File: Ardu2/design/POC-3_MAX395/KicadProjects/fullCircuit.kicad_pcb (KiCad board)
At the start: 2 copper layers, 179.3 x 143.5 mm, 131 parts, among them P1 CONN_01X02, P2 CONN_01X14, P3 CONN_01X14, P4 CONN_01X01, P7 CONN_01X15, U1 Pyboard, U10 MAX395, U11 MAX395, U12 MAX395, U13 MAX395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

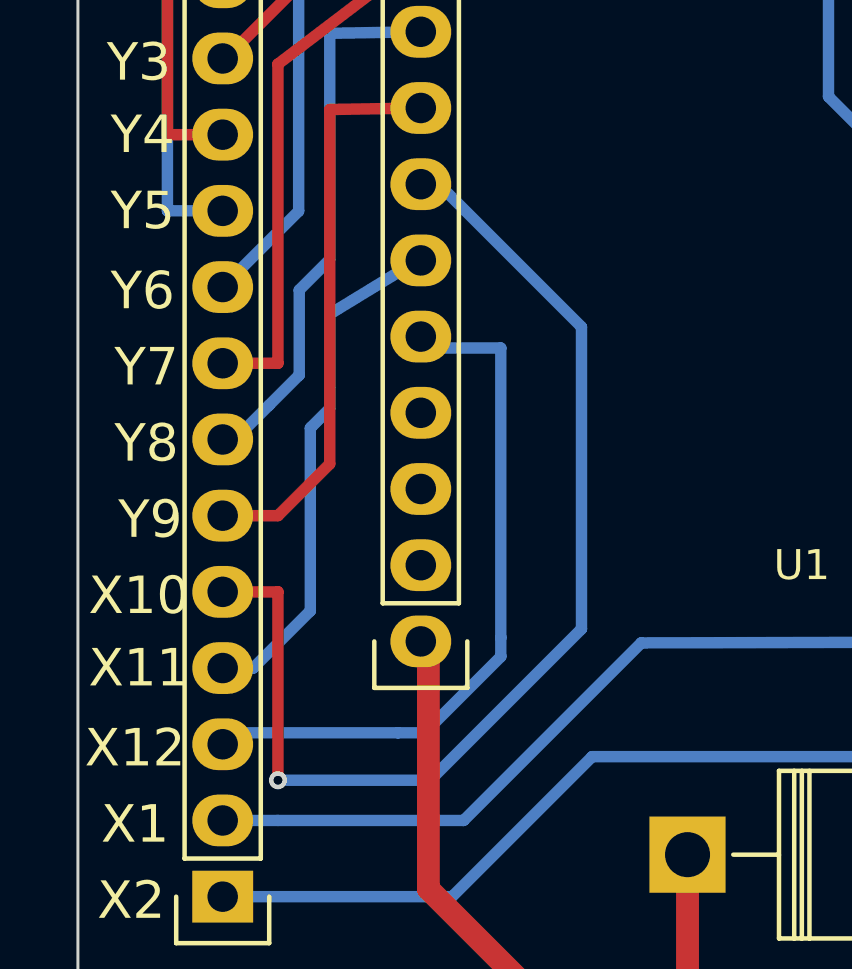
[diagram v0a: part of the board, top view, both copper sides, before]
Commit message: improved some pcb tracks
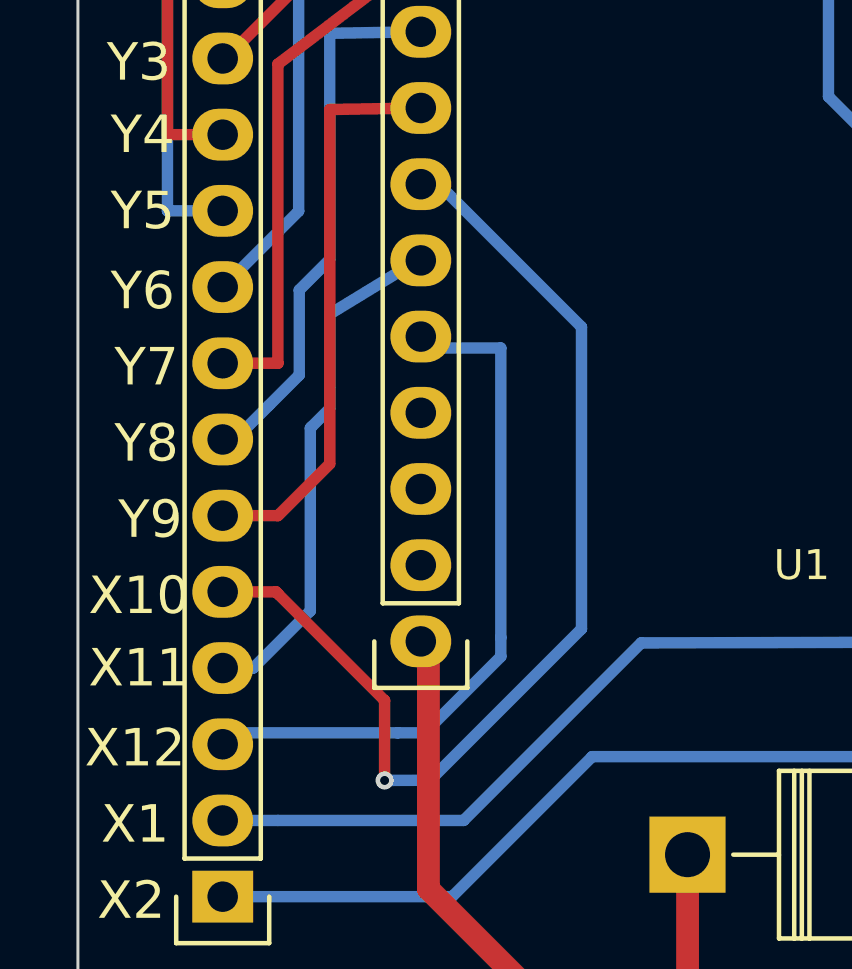
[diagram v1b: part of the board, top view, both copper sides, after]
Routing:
- net Net-(P2-Pad5): track 37.7 -> 35.6 mm
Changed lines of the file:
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@@
-(kicad_pcb (version 4) (host pcbnew 0.201506212247+5800~23~ubuntu15.04.1-product)
+(kicad_pcb (version 4) (host pcbnew 0.201509051501+6156~29~ubuntu15.04.1-product)
   (general
     (links 506)
@@
     (thickness 1.6)
     (drawings 44)
-    (tracks 1412)
+    (tracks 1414)
     (zones 0)
     (modules 131)
@@
   (segment (start 68.072 98.552) (end 67.056 98.552) (width 0.381) (layer B.Cu_SPI.VMinus) (net 109) (status 30))
   (segment (start 69.977 96.647) (end 68.072 98.552) (width 0.381) (layer B.Cu_SPI.VMinus) (net 109) (status 20))
-  (segment (start 68.8978 96.012) (end 68.8978 102.2916) (width 0.381) (layer F.Cu_Audio.GND) (net 110))
-  (segment (start 74.308 82.4738) (end 79.0165 87.1823) (width 0.381) (layer B.Cu_SPI.VMinus) (net 110))
-  (segment (start 79.0165 87.1823) (end 79.0165 97.247) (width 0.381) (layer B.Cu_SPI.VMinus) (net 110))
+  (segment (start 67.056 96.012) (end 68.834 96.012) (width 0.381) (layer F.Cu_Audio.GND) (net 110))
+  (segment (start 72.4535 99.6315) (end 68.8978 96.0758) (width 0.381) (layer F.Cu_Audio.GND) (net 110))
+  (via (at 72.4535 102.2985) (size 0.6) (layers F.Cu_Audio.GND B.Cu_SPI.VMinus) (net 110))
+  (segment (start 73.9719 102.2916) (end 72.4535 102.2985) (width 0.381) (layer B.Cu_SPI.VMinus) (net 110))
   (segment (start 79.0165 97.247) (end 73.9719 102.2916) (width 0.381) (layer B.Cu_SPI.VMinus) (net 110))
-  (segment (start 73.9719 102.2916) (end 68.8978 102.2916) (width 0.381) (layer B.Cu_SPI.VMinus) (net 110))
+  (segment (start 79.0165 87.1823) (end 79.0165 97.247) (width 0.381) (layer B.Cu_SPI.VMinus) (net 110))
+  (segment (start 79.0165 87.1823) (end 74.308 82.4738) (width 0.381) (layer B.Cu_SPI.VMinus) (net 110))
+  (segment (start 72.4535 102.2985) (end 72.4535 99.6315) (width 0.381) (layer F.Cu_Audio.GND) (net 110))
+  (segment (start 68.834 96.012) (end 68.8978 96.0758) (width 0.381) (layer F.Cu_Audio.GND) (net 110))
   (segment (start 73.66 82.423) (end 74.308 82.4738) (width 0.381) (layer B.Cu_SPI.VMinus) (net 110) (status 10))
-  (segment (start 67.056 96.012) (end 68.8978 96.012) (width 0.381) (layer F.Cu_Audio.GND) (net 110) (status 10))
-  (via (at 68.8978 102.2916) (size 0.6) (layers F.Cu_Audio.GND B.Cu_SPI.VMinus) (net 110))
   (segment (start 73.66 79.883) (end 70.6244 79.9338) (width 0.381) (layer F.Cu_Audio.GND) (net 111) (status 10))
   (segment (start 67.056 93.472) (end 68.8978 93.472) (width 0.381) (layer F.Cu_Audio.GND) (net 111) (status 10))

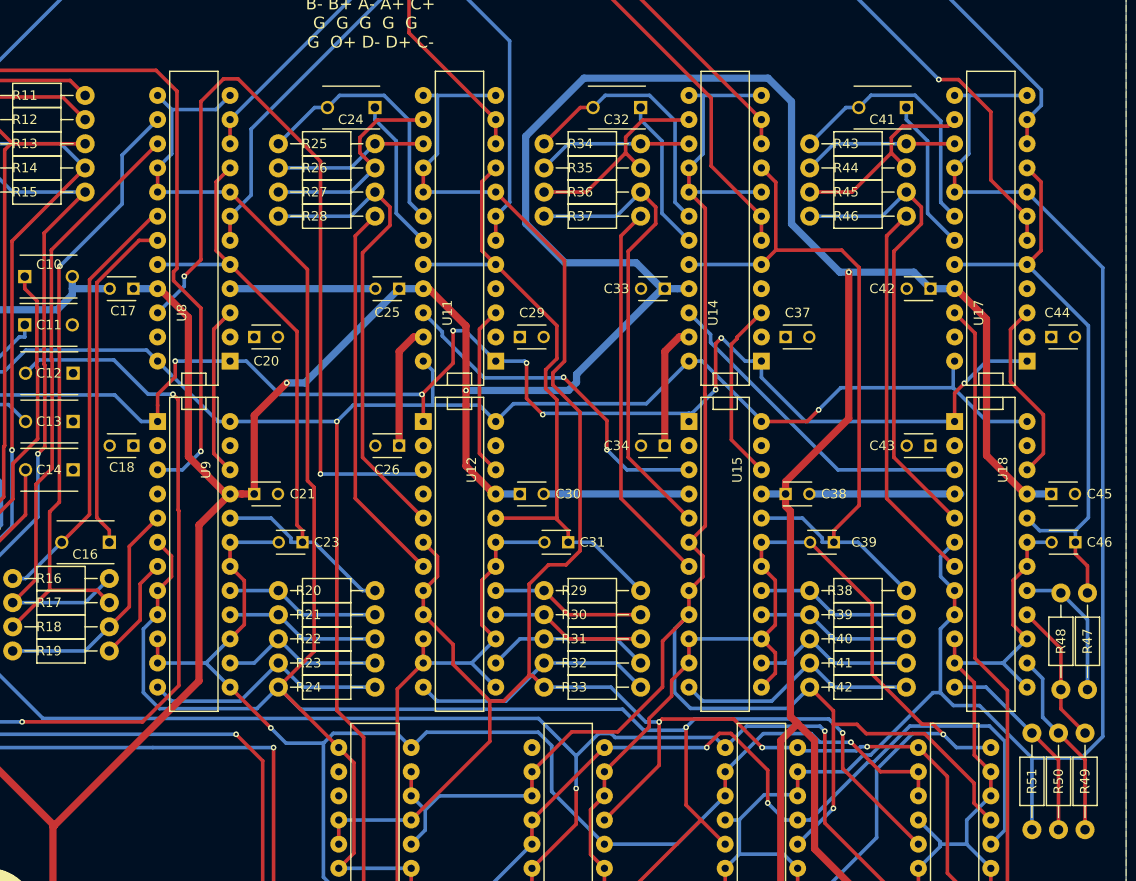
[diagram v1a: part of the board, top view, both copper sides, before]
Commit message: updates to PCB for EuroCircuits Fab
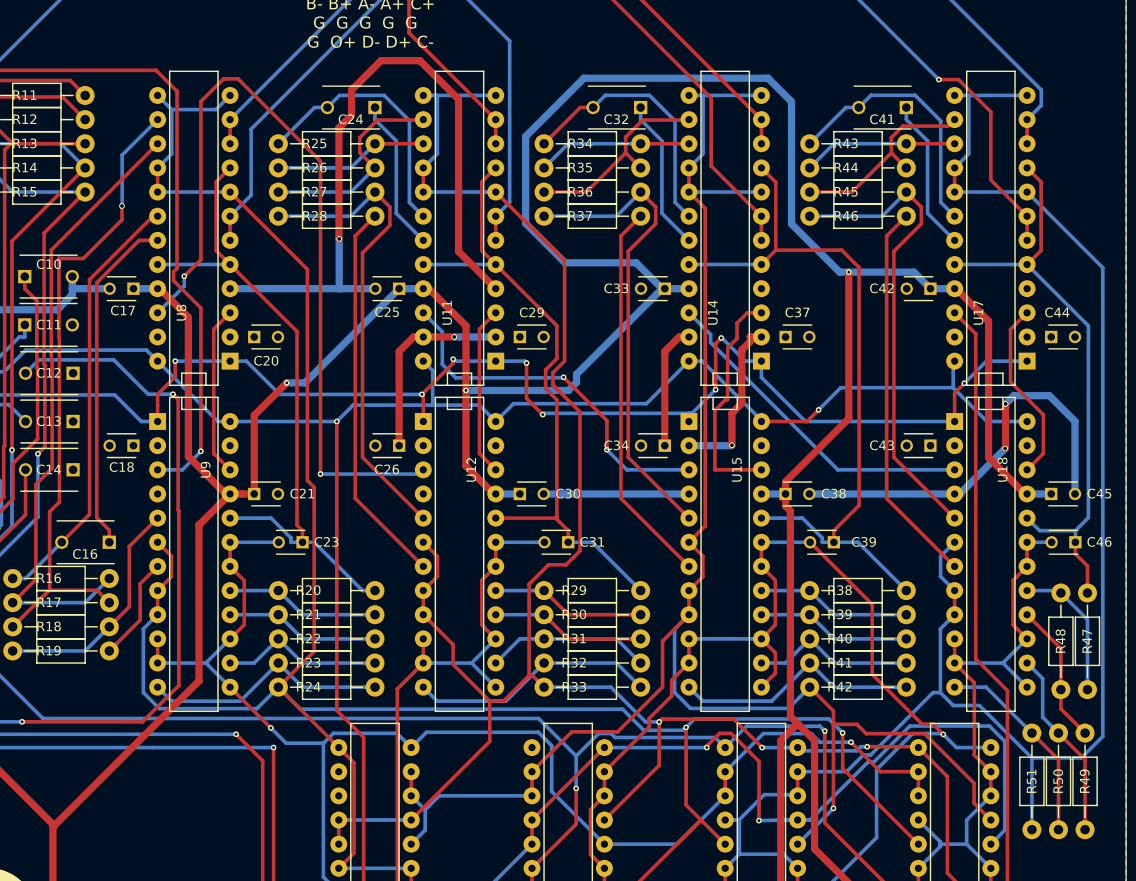
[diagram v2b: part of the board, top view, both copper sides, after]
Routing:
- net GND: track 72.1 -> 157.7 mm, vias 0 -> 3
- net /V+: track 79.5 -> 107.1 mm, vias 0 -> 2
- net Net-(U14-Pad3): track 19.1 -> 24.5 mm
- net /CLK: track 418.4 -> 414.1 mm
- net Net-(U11-Pad22): track 36.9 -> 38.6 mm
- net /COut+: track 161.3 -> 162.9 mm
- net Net-(R17-Pad2): track 66.5 -> 67.9 mm

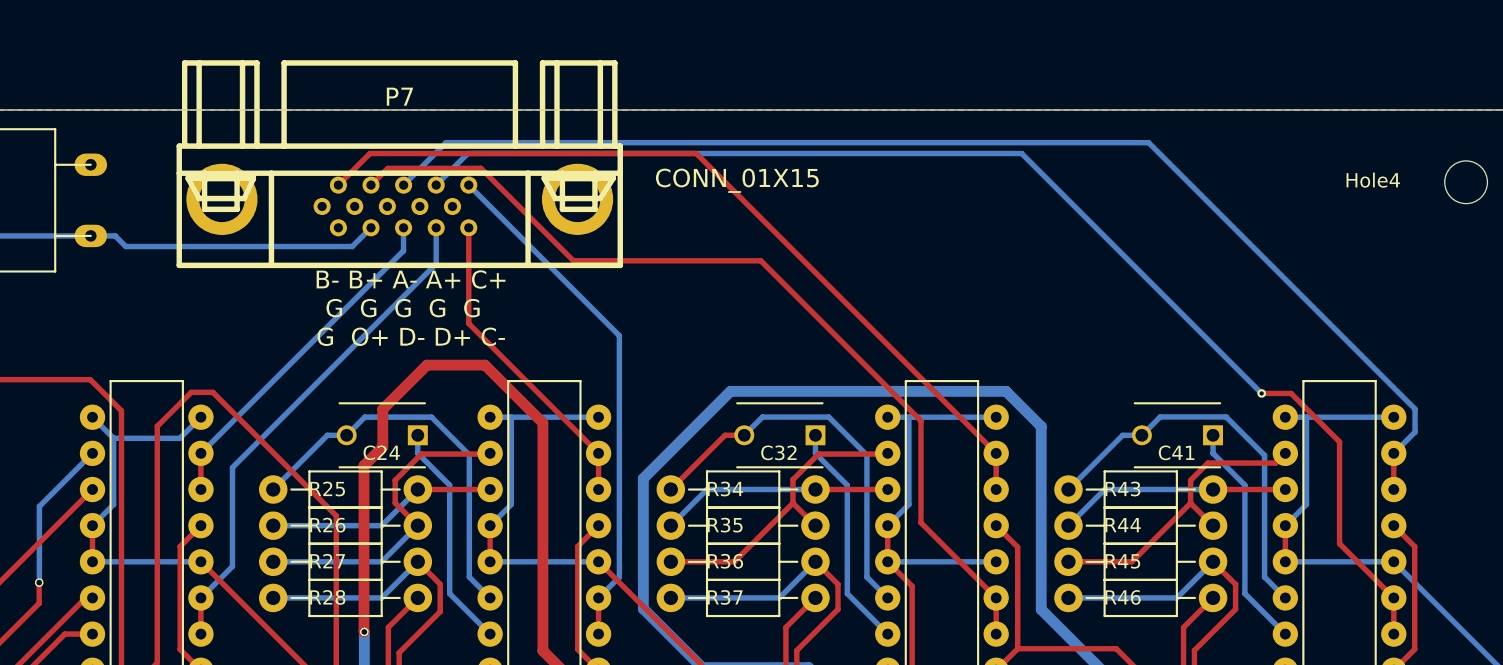
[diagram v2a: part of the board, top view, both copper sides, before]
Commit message: updates to the pcb layout this corresponds to the working prototype PCB
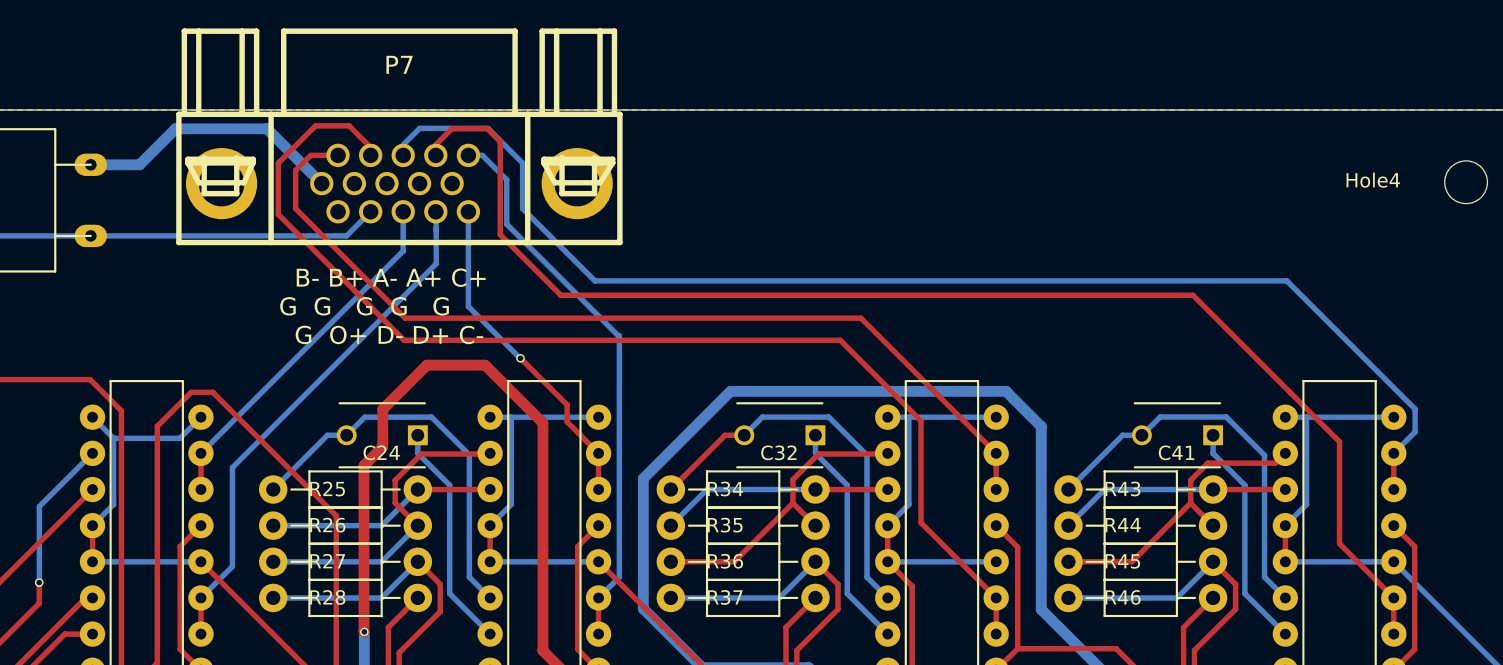
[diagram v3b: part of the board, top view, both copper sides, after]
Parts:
- P7: footprint w_conn_pc:DB_15F-VGA -> w_conn_pc:DB_15F-VGA_00_BOB
- moved P7 2.24 mm to (161.3, 19.4)
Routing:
- net GND: track 157.7 -> 176.6 mm
- net /B+: track 63.7 -> 80.7 mm
- net /B-: track 58.4 -> 65.0 mm
- net /A+: track 87.9 -> 92.7 mm, vias 1 -> 0
- net /C+: track 36.5 -> 39.3 mm
- net /A-: track 86.3 -> 88.6 mm
- net /D+: track 35.4 -> 36.8 mm
- net /C-: track 22.2 -> 23.3 mm, vias 0 -> 1
- net /D-: track 24.3 -> 25.4 mm

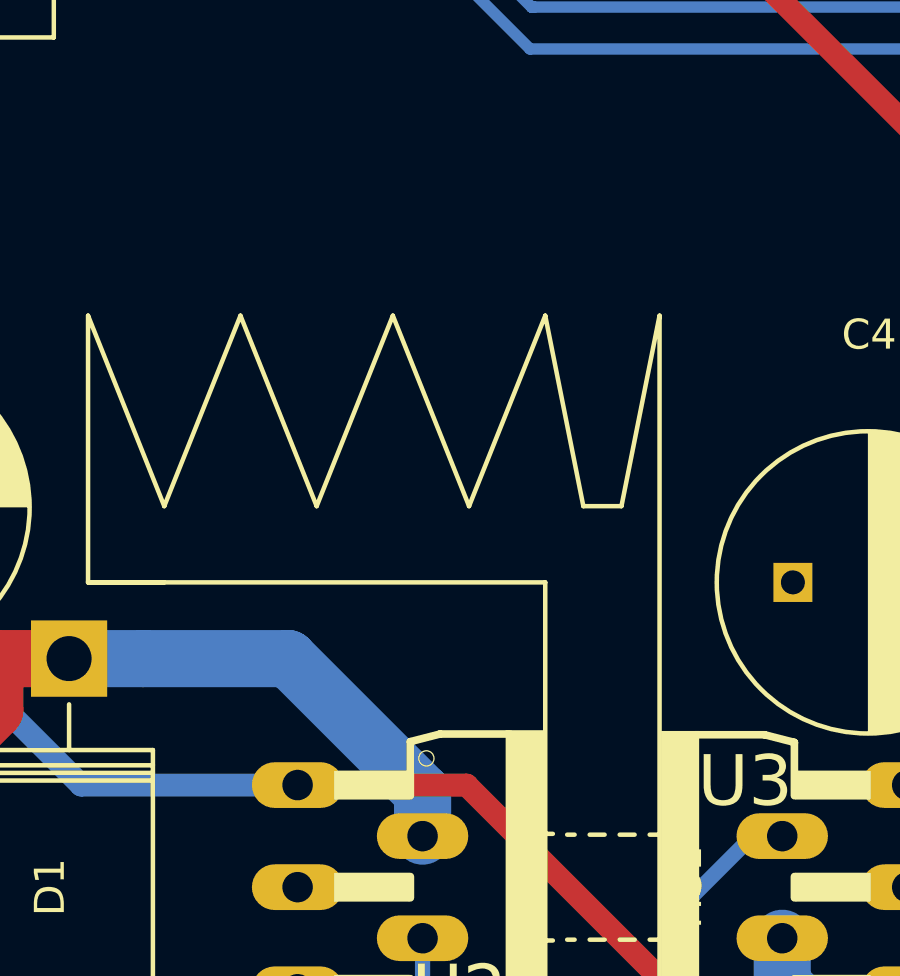
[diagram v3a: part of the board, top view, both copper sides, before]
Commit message: update to circuit for schottkey protection diode
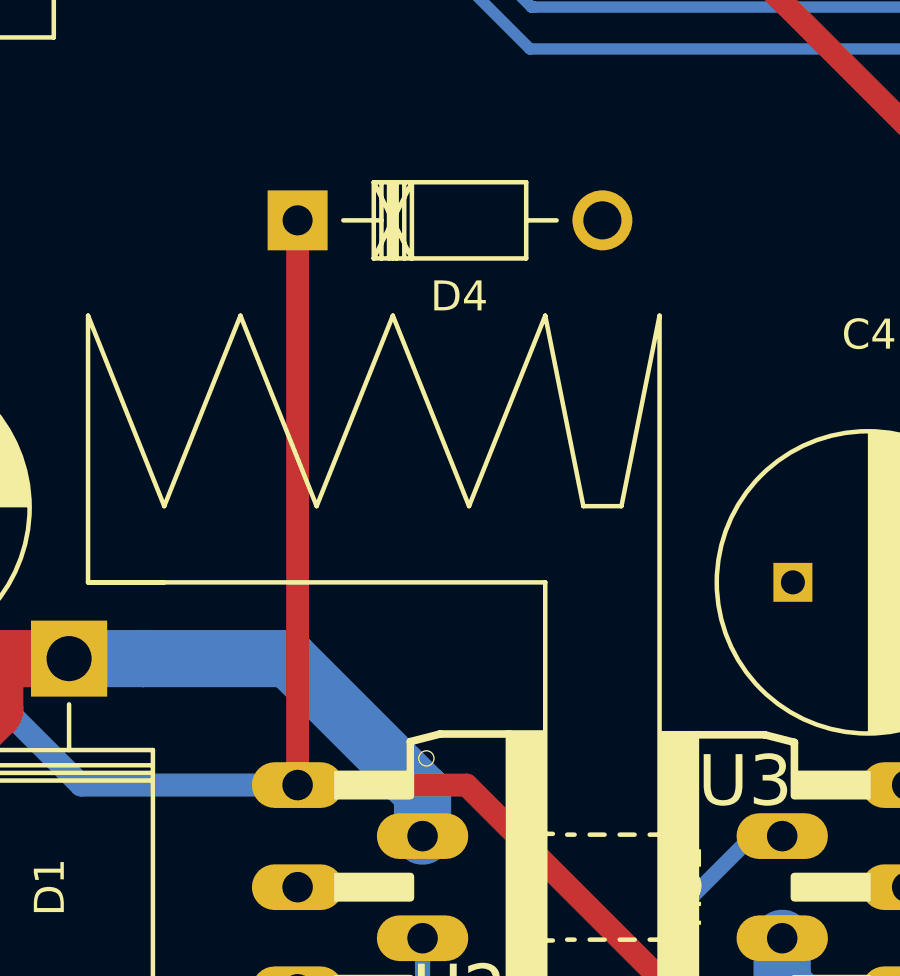
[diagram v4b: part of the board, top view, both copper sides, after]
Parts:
- added D4: D_Schottky UF-4003, Diodes_ThroughHole:Diode_DO-41_SOD81_Horizontal_RM10, F.Cu at (102.9, 113.7)
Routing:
- net /BATin: track 71.0 -> 89.8 mm
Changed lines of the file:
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@@
 (kicad_pcb (version 4) (host pcbnew 0.201511031201+6292~30~ubuntu15.04.1-product)
   (general
-    (links 506)
+    (links 508)
     (no_connects 0)
     (area 62.003238 11.417299 241.604001 161.340001)
     (thickness 1.6)
     (drawings 44)
-    (tracks 1490)
+    (tracks 1491)
     (zones 0)
-    (modules 131)
+    (modules 132)
     (nets 129)
   )
@@
   (title_block
     (title "Ardu2 MAX395 Full Circuit")
-    (date 2015-11-02)
-    (rev 1.7)
+    (date 2015-11-04)
+    (rev 1.8)
     (company www.arduguitar.org)
     (comment 1 "update after review,")
     (comment 2 "added V+/V- to headers")
     (comment 3 "updated VGC Connector footprint to match physical connector")
+    (comment 4 "added schottkey UF 4003 diode to prevent LM2956 latch-up")
   )
   (layers
-    (0 F.Cu_Audio.GND mixed hide)
-    (31 B.Cu_SPI.VMinus mixed hide)
+    (0 F.Cu_Audio.GND mixed)
+    (31 B.Cu_SPI.VMinus mixed)
     (33 F.Adhes user)
     (35 F.Paste user)
@@
     )
   )
+  (module Diodes_ThroughHole:Diode_DO-41_SOD81_Horizontal_RM10 (layer F.Cu_Audio.GND)
+    (at 102.87 113.665)
+    (descr "Diode, DO-41, SOD81, Horizontal, RM 10mm,")
+    (tags "Diode, DO-41, SOD81, Horizontal, RM 10mm, 1N4007, SB140,")
+    (fp_text reference D4 (at 5.38734 2.53746) (layer F.SilkS)
+      (effects (font (size 1 1) (thickness 0.15)))
+    )
+    (fp_text value "D_Schottky UF-4003" (at 4.37134 -3.55854) (layer F.Fab)
+      (effects (font (size 1 1) (thickness 0.15)))
+    )
+    (fp_line (start 7.62 -0.00254) (end 8.636 -0.00254) (layer F.SilkS) (width 0.15))
+    (fp_line (start 2.794 -0.00254) (end 1.524 -0.00254) (layer F.SilkS) (width 0.15))
+    (fp_line (start 3.048 -1.27254) (end 3.048 1.26746) (layer F.SilkS) (width 0.15))
+    (fp_line (start 3.302 -1.27254) (end 3.302 1.26746) (layer F.SilkS) (width 0.15))
+    (fp_line (start 3.556 -1.27254) (end 3.556 1.26746) (layer F.SilkS) (width 0.15))
+    (fp_line (start 2.794 -1.27254) (end 2.794 1.26746) (layer F.SilkS) (width 0.15))
+    (fp_line (start 3.81 -1.27254) (end 2.54 1.26746) (layer F.SilkS) (width 0.15))
+    (fp_line (start 2.54 -1.27254) (end 3.81 1.26746) (layer F.SilkS) (width 0.15))
+    (fp_line (start 3.81 -1.27254) (end 3.81 1.26746) (layer F.SilkS) (width 0.15))
+    (fp_line (start 3.175 -1.27254) (end 3.175 1.26746) (layer F.SilkS) (width 0.15))
+    (fp_line (start 2.54 1.26746) (end 2.54 -1.27254) (layer F.SilkS) (width 0.15))
+    (fp_line (start 2.54 -1.27254) (end 7.62 -1.27254) (layer F.SilkS) (width 0.15))
+    (fp_line (start 7.62 -1.27254) (end 7.62 1.26746) (layer F.SilkS) (width 0.15))
+    (fp_line (start 7.62 1.26746) (end 2.54 1.26746) (layer F.SilkS) (width 0.15))
+    (pad 2 thru_hole circle (at 10.16 -0.00254 180) (size 1.99898 1.99898) (drill 1.27) (layers *.Cu *.Mask F.SilkS)
+      (net 4 /V+))
+    (pad 1 thru_hole rect (at 0 -0.00254 180) (size 1.99898 1.99898) (drill 1.00076) (layers *.Cu *.Mask F.SilkS)
+      (net 1 /BATin))
+  )
   (gr_text V- (at 63.754 37.211) (layer F.SilkS)
     (effects (font (size 1.25 1.25) (thickness 0.2)))
@@
   (target plus (at 85.725 88.265) (size 5) (width 0.1) (layer Edge.Cuts))
   (target plus (at 236.855 40.767) (size 5) (width 0.1) (layer Edge.Cuts))
+  (segment (start 102.87 113.66246) (end 102.87 132.4864) (width 0.762) (layer F.Cu_Audio.GND) (net 1))
   (segment (start 102.87 132.4864) (end 95.6564 132.4864) (width 0.762) (layer B.Cu_SPI.VMinus) (net 1))
   (segment (start 95.6564 132.4864) (end 90.678 127.508) (width 0.762) (layer B.Cu_SPI.VMinus) (net 1))
